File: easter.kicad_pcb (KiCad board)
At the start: 2 copper layers, 69.7 x 90.8 mm, 27 parts, among them Q1 BC547, Q2 BC547, SW1 SW_Push_SPDT, SW2 Shake, SW3 SW_Push_SPDT

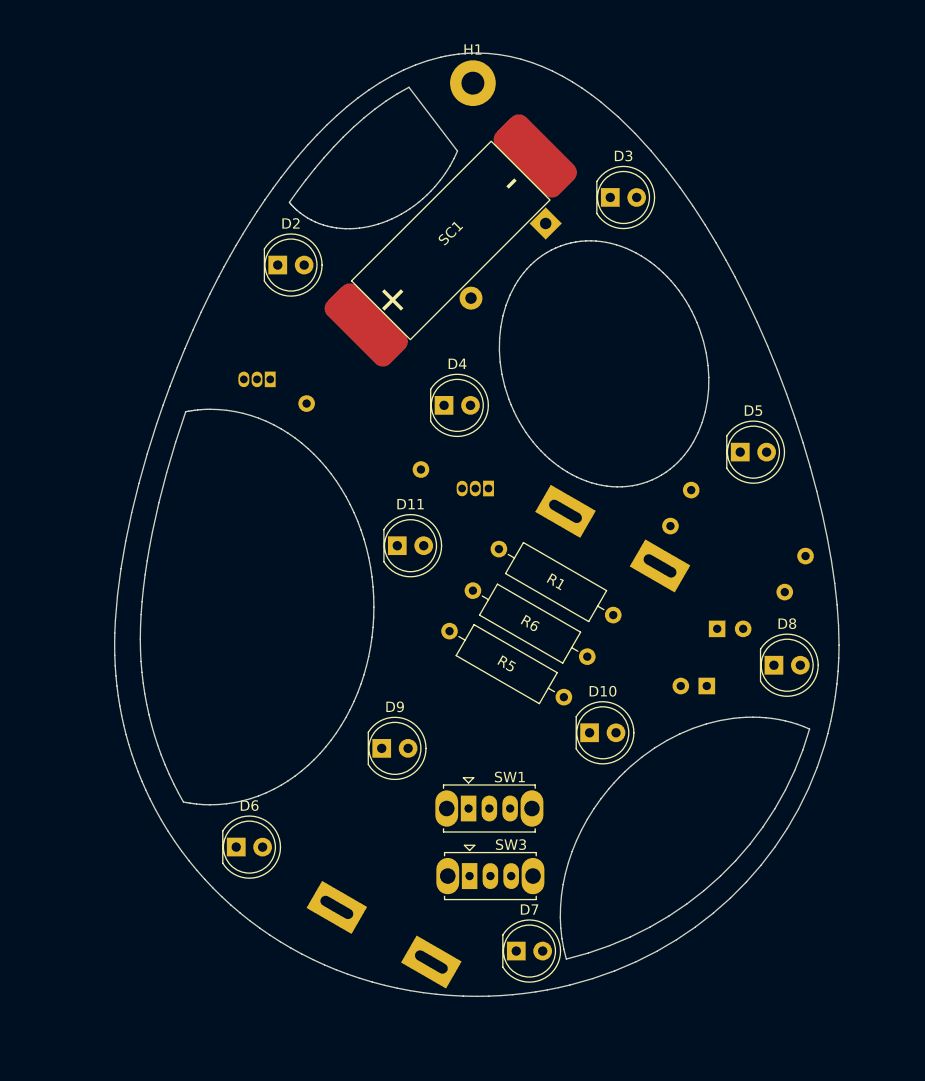
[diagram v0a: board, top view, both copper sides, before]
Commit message: Finish layout. Plot gerbers
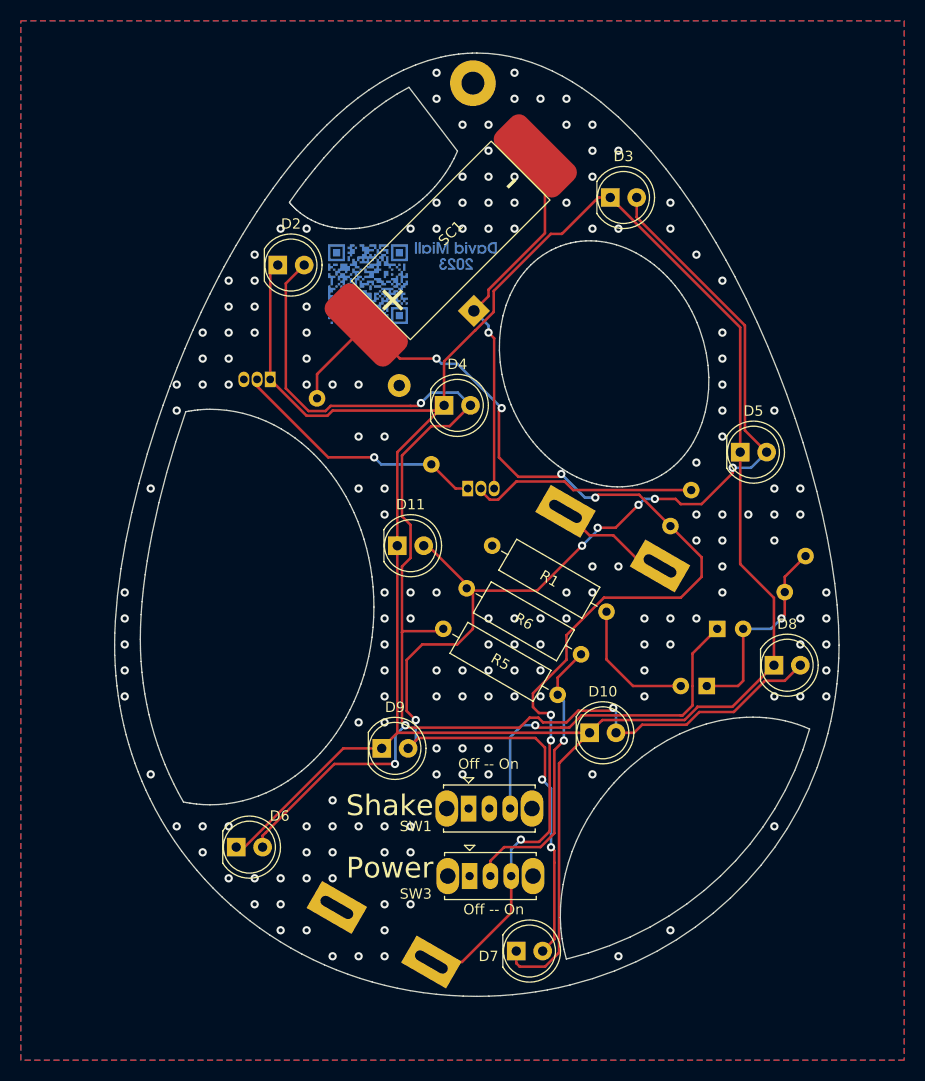
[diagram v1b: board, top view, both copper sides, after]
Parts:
- moved R4 12.1 mm to (108.5, 61.3), turned to -30 degrees
- moved D1 10.9 mm to (123.6, 52.9)
- moved Q1 2.00 mm to (123.0, 70.0), turned to 0 degrees
- moved R1 0.73 mm to (136.3, 81.8)
- moved R5 0.64 mm to (131.6, 89.8)
- moved R6 0.64 mm to (133.9, 86.0)
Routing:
- net Net-(D10-Pad1): track 0.00 -> 230.1 mm
- net Net-(D10-Pad2): track 0.00 -> 137.5 mm, vias 0 -> 4
- net Net-(D11-Pad2): track 0.00 -> 125.9 mm, vias 0 -> 8
- net VDC: track 0.00 -> 113.3 mm, vias 0 -> 7
- net Net-(D1-Pad1): track 0.00 -> 36.0 mm, vias 0 -> 1
- net Net-(SW1-Pad3): track 0.00 -> 34.2 mm, vias 0 -> 1
- net Net-(R5-Pad1): track 0.00 -> 27.5 mm, vias 0 -> 1
- net Net-(Q1-Pad1): track 0.00 -> 25.0 mm, vias 0 -> 1
- net Net-(Q1-Pad2): track 0.00 -> 21.9 mm
- net Net-(C1-Pad1): track 0.00 -> 19.8 mm, vias 0 -> 1
- net Net-(C1-Pad2): track 0.00 -> 12.8 mm
- net Net-(BT1-Pad2): track 0.00 -> 11.3 mm
- net GND: vias 0 -> 172
- added copper zone on B.Cu, net GND
- added copper zone on F.Cu, net GND
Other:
- board text added: "Off -- On"
- board text added: "Power"
- board text added: "Shake"

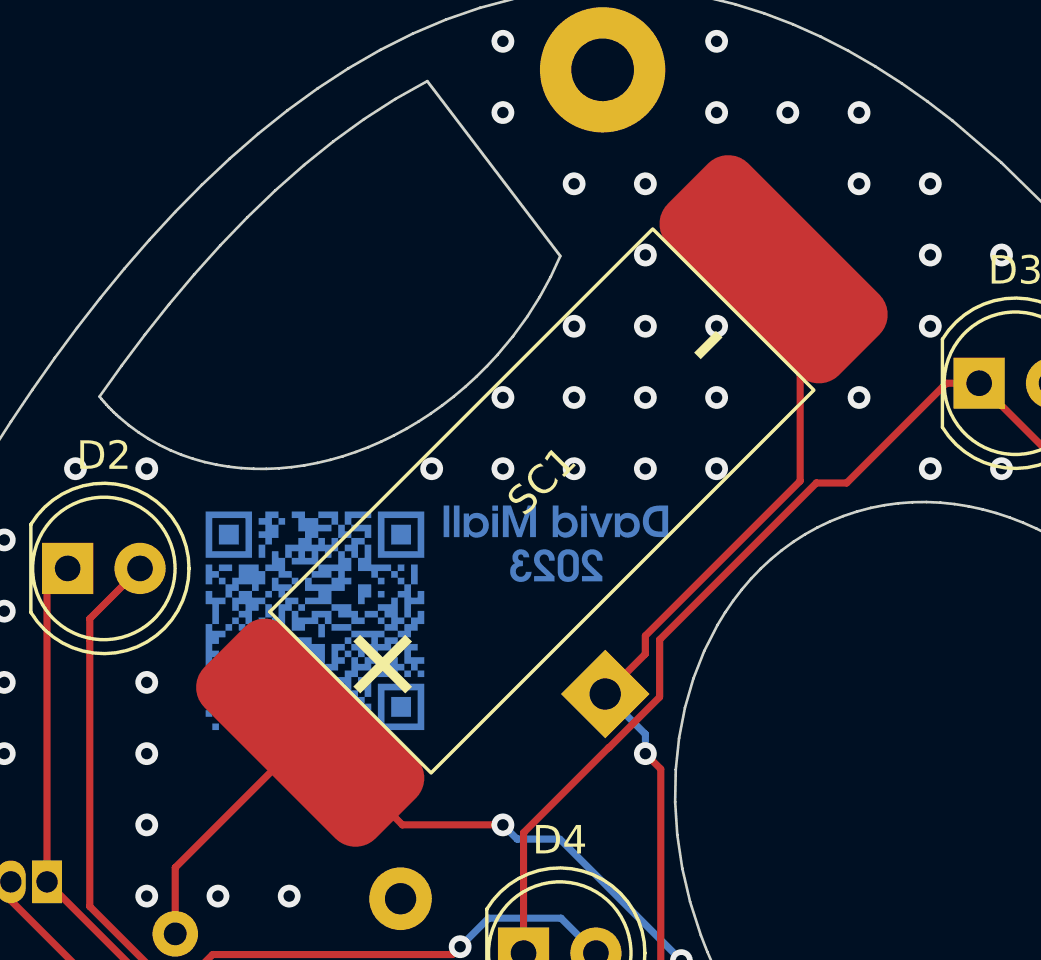
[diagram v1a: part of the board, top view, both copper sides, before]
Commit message: Add solar test points
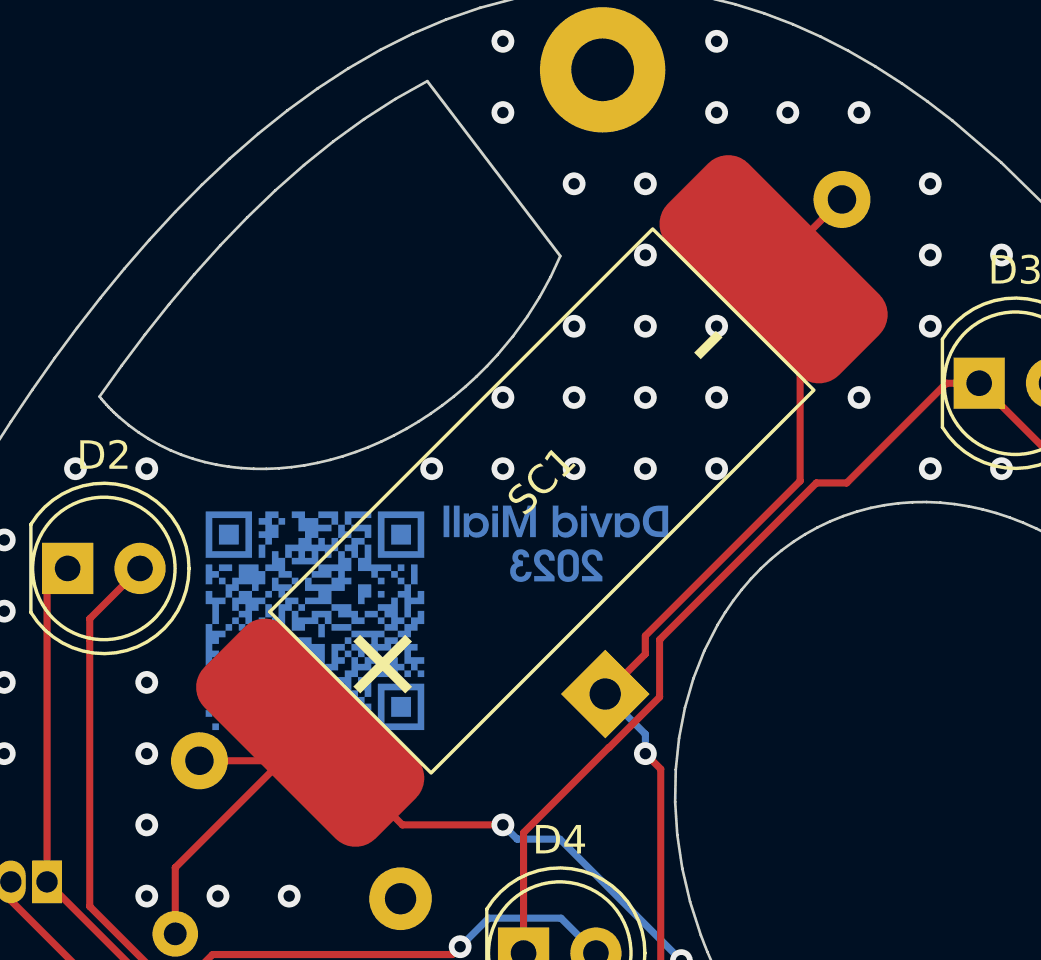
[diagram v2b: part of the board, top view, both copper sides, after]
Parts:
- added TP1: TestPoint, TestPoint:TestPoint_THTPad_D2.0mm_Drill1.0mm, B.Cu at (109.3, 55.2)
- added TP2: TestPoint, TestPoint:TestPoint_THTPad_D2.0mm_Drill1.0mm, B.Cu at (131.9, 35.5)
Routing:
- net VDC: track 113.3 -> 117.6 mm
- net Net-(D1-Pad1): track 36.0 -> 39.5 mm
- net GND: vias 172 -> 171
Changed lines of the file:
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@@
       (outputformat 1)
       (mirror false)
-      (drillshape 1)
+      (drillshape 0)
       (scaleselection 1)
       (outputdirectory "")
@@
     )
   )
+  (footprint "TestPoint:TestPoint_THTPad_D2.0mm_Drill1.0mm" (layer "B.Cu")
+    (at 131.9 35.55 180)
+    (descr "THT pad as test Point, diameter 2.0mm, hole diameter 1.0mm")
+    (tags "test point THT pad")
+    (property "Sheetfile" "easter.kicad_sch")
+    (property "Sheetname" "")
+    (attr exclude_from_pos_files)
+    (fp_text reference "TP2" (at 0 1.998) (layer "B.SilkS")
+      (effects (font (size 1 1) (thickness 0.15)) (justify mirror))
+    )
+    (fp_text value "TestPoint" (at 0 -2.05) (layer "B.Fab")
+      (effects (font (size 1 1) (thickness 0.15)) (justify mirror))
+    )
+    (fp_text user "${REFERENCE}" (at 0 2) (layer "B.Fab")
+      (effects (font (size 1 1) (thickness 0.15)) (justify mirror))
+    )
+    (fp_circle (center 0 0) (end 0 -1.2) (layer "B.SilkS") (width 0.12) (fill none))
+    (fp_circle (center 0 0) (end 1.5 0) (layer "B.CrtYd") (width 0.05) (fill none))
+    (pad "1" thru_hole circle (at 0 0 180) (size 2 2) (drill 1) (layers *.Cu *.Mask)
+      (net 6 "Net-(D1-Pad1)") (pinfunction "1") (pintype "passive"))
+  )
   (footprint "custom footprints:MP001179" (layer "B.Cu")
     (at 119.5 115.552559 60)
@@
     )
   )
+  (footprint "TestPoint:TestPoint_THTPad_D2.0mm_Drill1.0mm" (layer "B.Cu")
+    (at 109.35 55.25 180)
+    (descr "THT pad as test Point, diameter 2.0mm, hole diameter 1.0mm")
+    (tags "test point THT pad")
+    (property "Sheetfile" "easter.kicad_sch")
+    (property "Sheetname" "")
+    (attr exclude_from_pos_files)
+    (fp_text reference "TP1" (at 2.15 -1.75) (layer "B.SilkS")
+      (effects (font (size 1 1) (thickness 0.15)) (justify mirror))
+    )
+    (fp_text value "TestPoint" (at 0 -2.05) (layer "B.Fab")
+      (effects (font (size 1 1) (thickness 0.15)) (justify mirror))
+    )
+    (fp_text user "${REFERENCE}" (at 0 2) (layer "B.Fab")
+      (effects (font (size 1 1) (thickness 0.15)) (justify mirror))
+    )
+    (fp_circle (center 0 0) (end 0 -1.2) (layer "B.SilkS") (width 0.12) (fill none))
+    (fp_circle (center 0 0) (end 1.5 0) (layer "B.CrtYd") (width 0.05) (fill none))
+    (pad "1" thru_hole circle (at 0 0 180) (size 2 2) (drill 1) (layers *.Cu *.Mask)
+      (net 1 "VDC") (pinfunction "1") (pintype "passive"))
+  )
   (footprint "Capacitor_THT:CP_Radial_D5.0mm_P2.50mm" (layer "B.Cu")
     (at 147 83.5)
@@
   (segment (start 127.18 110.82) (end 127.18 107.285) (width 0.25) (layer "F.Cu") (net 1))
   (segment (start 129.275 91.025) (end 129.275 89.699695) (width 0.25) (layer "F.Cu") (net 1))
+  (segment (start 109.35 55.25) (end 112.25 55.25) (width 0.25) (layer "F.Cu") (net 1))
   (segment (start 129.275 89.699695) (end 132.5 86.474695) (width 0.25) (layer "F.Cu") (net 1))
   (segment (start 143.5 80.5) (end 145.5 78.5) (width 0.25) (layer "F.Cu") (net 1))
@@
   (segment (start 131 94.2245) (end 130.882343 94.342157) (width 0.25) (layer "F.Cu") (net 1))
   (segment (start 108.500739 61.325) (end 108.500739 58.999261) (width 0.25) (layer "F.Cu") (net 1))
+  (segment (start 112.25 55.25) (end 113.236544 54.263456) (width 0.25) (layer "F.Cu") (net 1))
   (segment (start 145.5 76.612625) (end 142.501477 73.614102) (width 0.25) (layer "F.Cu") (net 1))
   (segment (start 136.109009 80.5) (end 143.5 80.5) (width 0.25) (layer "F.Cu") (net 1))
@@
   (via (at 112.5 92.5) (size 0.8) (drill 0.4) (layers "F.Cu" "B.Cu") (free) (net 3))
   (via (at 115 70) (size 0.8) (drill 0.4) (layers "F.Cu" "B.Cu") (free) (net 3))
-  (via (at 132.5 35) (size 0.8) (drill 0.4) (layers "F.Cu" "B.Cu") (free) (net 3))
   (via (at 157.5 80) (size 0.8) (drill 0.4) (layers "F.Cu" "B.Cu") (free) (net 3))
   (via (at 147.5 72.5) (size 0.8) (drill 0.4) (layers "F.Cu" "B.Cu") (free) (net 3))
@@
   (segment (start 125.54 70) (end 125.54 55.54) (width 0.25) (layer "F.Cu") (net 6))
   (segment (start 125 50.863604) (end 130.431802 45.431802) (width 0.25) (layer "F.Cu") (net 6))
+  (segment (start 129.5 37.95) (end 129.5 38) (width 0.25) (layer "F.Cu") (net 6))
+  (segment (start 131.9 35.55) (end 129.5 37.95) (width 0.25) (layer "F.Cu") (net 6))
   (via (at 125 55) (size 0.8) (drill 0.4) (layers "F.Cu" "B.Cu") (net 6))
   (segment (start 125 54.315795) (end 123.592103 52.907898) (width 0.25) (layer "B.Cu") (net 6))

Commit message: Fix trace
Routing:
- net Net-(D10-Pad1): track 230.1 -> 229.4 mm
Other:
- board text added: "JLCJLCJLCJLC"
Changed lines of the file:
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@@
   (gr_line (start 96.156145 62.558548) (end 96.442458 62.513603) (layer "Edge.Cuts") (width 0.092604))
   (gr_line (start 121.263789 28.329714) (end 120.837268 28.409766) (layer "Edge.Cuts") (width 0.092604))
+  (gr_text "JLCJLCJLCJLC" (at 113.157 103.759) (layer "B.SilkS")
+    (effects (font (size 0.9 0.9) (thickness 0.2)) (justify mirror))
+  )
   (gr_text "Power" (at 115.5 106.5) (layer "F.SilkS")
     (effects (font (size 2 2) (thickness 0.15)))
@@
   (segment (start 125 55) (end 125 54.315795) (width 0.25) (layer "B.Cu") (net 6))
   (segment (start 123.726724 54.788533) (end 123.711467 54.788533) (width 0.25) (layer "F.Cu") (net 7))
-  (segment (start 130.442412 116) (end 128 116) (width 0.25) (layer "F.Cu") (net 7))
   (segment (start 125.5 51) (end 125.5 53.015257) (width 0.25) (layer "F.Cu") (net 7))
-  (segment (start 128 116) (end 127.67 115.67) (width 0.25) (layer "F.Cu") (net 7))
+  (segment (start 134.725 93.5) (end 131.782343 96.442657) (width 0.25) (layer "F.Cu") (net 7))
+  (segment (start 131.435 113.992588) (end 131.435 115.007412) (width 0.25) (layer "F.Cu") (net 7))
   (segment (start 145.075 91.061396) (end 145.075 91) (width 0.25) (layer "F.Cu") (net 7))
   (segment (start 101.532588 104.5) (end 100.725 104.5) (width 0.25) (layer "F.Cu") (net 7))
@@
   (segment (start 109.5 63) (end 110 62.5) (width 0.25) (layer "F.Cu") (net 7))
   (segment (start 134.725 93.5) (end 135.95 92.275) (width 0.25) (layer "F.Cu") (net 7))
+  (segment (start 131.387 105.162903) (end 131.387 113.944588) (width 0.25) (layer "F.Cu") (net 7))
   (segment (start 104 59.5) (end 107.5 63) (width 0.25) (layer "F.Cu") (net 7))
   (segment (start 125.5 53.015257) (end 123.726724 54.788533) (width 0.25) (layer "F.Cu") (net 7))
   (segment (start 149.215 54.5) (end 136.715 42) (width 0.25) (layer "F.Cu") (net 7))
   (segment (start 116.225 75.5) (end 116.225 93.5) (width 0.25) (layer "F.Cu") (net 7))
-  (segment (start 131.782343 114.660069) (end 130.442412 116) (width 0.25) (layer "F.Cu") (net 7))
   (segment (start 131 45.5) (end 125.5 51) (width 0.25) (layer "F.Cu") (net 7))
   (segment (start 104 59.5) (end 104 49.225) (width 0.25) (layer "F.Cu") (net 7))
   (segment (start 149.215 77.270093) (end 149.215 66.5) (width 0.25) (layer "F.Cu") (net 7))
   (segment (start 152.46 80.515093) (end 149.215 77.270093) (width 0.25) (layer "F.Cu") (net 7))
+  (segment (start 131.435 115.007412) (end 130.442412 116) (width 0.25) (layer "F.Cu") (net 7))
+  (segment (start 130.442412 116) (end 129.17 116) (width 0.25) (layer "F.Cu") (net 7))
+  (segment (start 129.17 116) (end 127.67 114.5) (width 0.25) (layer "F.Cu") (net 7))
+  (segment (start 131.782343 104.76756) (end 131.387 105.162903) (width 0.25) (layer "F.Cu") (net 7))
   (segment (start 143.861396 92.275) (end 145.075 91.061396) (width 0.25) (layer "F.Cu") (net 7))
   (segment (start 123.711467 54.788533) (end 120.725 57.775) (width 0.25) (layer "F.Cu") (net 7))
   (segment (start 116.225 93.5) (end 114.725 95) (width 0.25) (layer "F.Cu") (net 7))
-  (segment (start 131.782343 96.442657) (end 131.782343 114.660069) (width 0.25) (layer "F.Cu") (net 7))
   (segment (start 116.225 66.5) (end 120.725 62) (width 0.25) (layer "F.Cu") (net 7))
   (segment (start 132.065 45.5) (end 131 45.5) (width 0.25) (layer "F.Cu") (net 7))
-  (segment (start 127.67 115.67) (end 127.67 114.5) (width 0.25) (layer "F.Cu") (net 7))
   (segment (start 120.725 57.775) (end 120.725 62) (width 0.25) (layer "F.Cu") (net 7))
   (segment (start 145.075 91) (end 148.46 91) (width 0.25) (layer "F.Cu") (net 7))
   (segment (start 135.95 92.275) (end 143.861396 92.275) (width 0.25) (layer "F.Cu") (net 7))
-  (segment (start 134.725 93.5) (end 131.782343 96.442657) (width 0.25) (layer "F.Cu") (net 7))
   (segment (start 114.725 95) (end 111.032588 95) (width 0.25) (layer "F.Cu") (net 7))
   (segment (start 110 62.5) (end 120.225 62.5) (width 0.25) (layer "F.Cu") (net 7))
+  (segment (start 131.782343 96.442657) (end 131.782343 104.76756) (width 0.25) (layer "F.Cu") (net 7))
   (segment (start 120.225 62.5) (end 120.725 62) (width 0.25) (layer "F.Cu") (net 7))
+  (segment (start 131.387 113.944588) (end 131.435 113.992588) (width 0.25) (layer "F.Cu") (net 7))
   (segment (start 111.032588 95) (end 101.532588 104.5) (width 0.25) (layer "F.Cu") (net 7))
   (segment (start 107.5 63) (end 109.5 63) (width 0.25) (layer "F.Cu") (net 7))
@@
   (segment (start 129.675 79.825) (end 123.500738 79.825) (width 0.25) (layer "F.Cu") (net 13))
   (segment (start 148.4905 68.5095) (end 145.5 71.5) (width 0.25) (layer "F.Cu") (net 13))
-  (segment (start 131.332343 104.832343) (end 131.012299 104.512299) (width 0.25) (layer "F.Cu") (net 13))
+  (segment (start 130.937 104.587598) (end 131.012299 104.512299) (width 0.25) (layer "F.Cu") (net 13))
   (segment (start 117.125 86.5) (end 118.625 85) (width 0.25) (layer "F.Cu") (net 13))
+  (segment (start 130.21 114.5) (end 130.937 113.773) (width 0.25) (layer "F.Cu") (net 13))
   (segment (start 118 92.2755) (end 117.125 91.4005) (width 0.25) (layer "F.Cu") (net 13))
-  (segment (start 130.21 114.5) (end 131.332343 113.377657) (width 0.25) (layer "F.Cu") (net 13))
   (segment (start 130.432343 94.932343) (end 129.5 94) (width 0.25) (layer "F.Cu") (net 13))
   (segment (start 118.625 85) (end 122 85) (width 0.25) (layer "F.Cu") (net 13))
   (segment (start 123.500738 83.499262) (end 123.500738 79.825) (width 0.25) (layer "F.Cu") (net 13))
   (segment (start 139.431388 71.568612) (end 137.2245 73.7755) (width 0.25) (layer "F.Cu") (net 13))
-  (segment (start 131.332343 113.377657) (end 131.332343 106) (width 0.25) (layer "F.Cu") (net 13))
   (segment (start 129.5 94) (end 118.265 94) (width 0.25) (layer "F.Cu") (net 13))
   (segment (start 149.665 64.41) (end 149.665 54.313604) (width 0.25) (layer "F.Cu") (net 13))
@@
   (segment (start 151.755 66.5) (end 149.665 64.41) (width 0.25) (layer "F.Cu") (net 13))
   (segment (start 130.432343 97.7255) (end 130.432343 94.932343) (width 0.25) (layer "F.Cu") (net 13))
+  (segment (start 130.937 113.773) (end 130.937 104.587598) (width 0.25) (layer "F.Cu") (net 13))
   (segment (start 119.175738 75.5) (end 118.765 75.5) (width 0.25) (layer "F.Cu") (net 13))
   (segment (start 137.2245 73.7755) (end 135.5 73.7755) (width 0.25) (layer "F.Cu") (net 13))
@@
   (segment (start 130.157843 98) (end 130.432343 97.7255) (width 0.25) (layer "F.Cu") (net 13))
   (segment (start 117.125 91.4005) (end 117.125 86.5) (width 0.25) (layer "F.Cu") (net 13))
-  (segment (start 131.332343 106) (end 131.332343 104.832343) (width 0.25) (layer "F.Cu") (net 13))
   (segment (start 143 71) (end 141 71) (width 0.25) (layer "F.Cu") (net 13))
   (segment (start 149.665 54.313604) (end 139.255 43.903604) (width 0.25) (layer "F.Cu") (net 13))
